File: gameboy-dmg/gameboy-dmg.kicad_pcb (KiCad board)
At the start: 2 copper layers, 82 x 63.5 mm, 27 parts, among them J1 Conn_01x02, J2 Conn_01x06, J3 Conn_01x02, SW1 SW_Push, SW2 SW_Push, SW3 SW_Push, SW4 SW_Push, SW5 SW_Push, SW6 SW_Push, SW7 SW_Push, SW8 SW_Push, U1 MCP23017_SO

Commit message: Added some graphics and stuffs
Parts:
- added G***: LOGO, pad:Tux, B.Cu at (135.7, 106.8)
- added G***: LOGO, pad:RetroPie_logo, B.Cu at (180.5, 102.5)
- C1: value C_Small -> 33nF
- C2: value C_Small -> 10uF
- R1: value R -> 270R
- R2: value R -> 150R
- moved J3 5.60 mm to (184.8, 75.4)
- renumbered SW8 to A1, SW7 to B1, SW3 to DOWN1, SW1 to LEFT1, SW4 to RIGHT1, SW5 to SELECT1, SW6 to START1, SW2 to UP1
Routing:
- net Net-(J3-Pad1): track 16.8 -> 20.9 mm
- net Net-(J3-Pad2): track 14.1 -> 17.2 mm
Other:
- board text added: "5V POWAH"
- board text added: "EXTRA BUTTONS"
- board text added: "GROUND"
- board text added: "INTERRUPT A"
- board text added: "INTERRUPT B"
- board text added: "SCK"
- board text added: "SDA"

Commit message: Added some more bits
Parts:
- added D1: LED, LED_SMD:LED_0603_1608Metric, F.Cu at (133.7, 72.2)
- added D2: LED, LED_THT:LED_D3.0mm, F.Cu at (134.9, 65.2)
- added J4: Conn_01x02, Connector_PinHeader_2.54mm:PinHeader_1x02_P2.54mm_Vertical, F.Cu at (127.3, 119.9)
- added J5: Raspberry_Pi_2_3, Connector_PinHeader_2.54mm:PinHeader_2x20_P2.54mm_Vertical, F.Cu at (185.9, 72.6)
- added J6: Conn_01x09, Connector_PinHeader_2.54mm:PinHeader_1x09_P2.54mm_Vertical, F.Cu at (147.8, 79.3)
- added JP1: SolderJumper_2_Bridged, Jumper:SolderJumper-2_P1.3mm_Bridged_RoundedPad1.0x1.5mm, F.Cu at (133.1, 78.3)
- added JP2: SolderJumper_2_Open, Jumper:SolderJumper-2_P1.3mm_Open_RoundedPad1.0x1.5mm, F.Cu at (184.8, 89.4)
- added JP3: SolderJumper_2_Open, Jumper:SolderJumper-2_P1.3mm_Open_RoundedPad1.0x1.5mm, F.Cu at (184.8, 85.3)
- added JP4: SolderJumper_2_Open, Jumper:SolderJumper-2_P1.3mm_Open_RoundedPad1.0x1.5mm, F.Cu at (179.0, 85.3)
- added JP5: SolderJumper_2_Open, Jumper:SolderJumper-2_P1.3mm_Open_RoundedPad1.0x1.5mm, F.Cu at (179.0, 89.6)
- added JP6: SolderJumper_2_Open, Jumper:SolderJumper-2_P1.3mm_Open_RoundedPad1.0x1.5mm, F.Cu at (142.3, 80.9)
- added JP7: SolderJumper_2_Bridged, Jumper:SolderJumper-2_P1.3mm_Bridged_RoundedPad1.0x1.5mm, F.Cu at (142.3, 78.4)
- added JP8: SolderJumper_2_Open, Jumper:SolderJumper-2_P1.3mm_Open_RoundedPad1.0x1.5mm, F.Cu at (129.4, 73.4)
- added R3: R_Small, Resistor_SMD:R_0603_1608Metric, F.Cu at (131.8, 72.2)
- added REF**: MountingHole_4.5mm, MountingHole:MountingHole_4.5mm, F.Cu at (127.5, 62.5)
- added REF**: MountingHole_4.5mm, MountingHole:MountingHole_4.5mm, F.Cu at (201.5, 62.5)
- added SW1: SW_DIP_x01, Connector_PinHeader_2.54mm:PinHeader_1x02_P2.54mm_Vertical, F.Cu at (125.8, 74.0)
- C2: moved to F.Cu
- J2: value Conn_01x06 -> Conn_01x02; footprint Connector_PinHeader_2.54mm:PinHeader_1x06_P2.54mm_Vertical -> Connector_PinHeader_2.54mm:PinHeader_1x02_P2.54mm_Vertical
- moved J2 60.7 mm to (142.5, 133.3), turned to 270 degrees
- moved R1 25.0 mm to (161.5, 125.5), turned to 90 degrees
- moved C2 24.5 mm to (163.2, 131.9), turned to 90 degrees
- moved C1 24.0 mm to (162.6, 122.9)
- moved R2 23.0 mm to (163.8, 125.5), turned to 90 degrees
- moved J1 18.5 mm to (168.0, 126.5), turned to 165 degrees
- moved J3 13.2 mm to (196.8, 80.8), turned to 180 degrees
- moved U1 11.0 mm to (164.4, 97.7), turned to 180 degrees
- moved G*** 6.02 mm to (176.5, 107.0)
- moved G*** 0.22 mm to (135.9, 106.7)
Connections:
- J1 pad 2: /PWM_IN -> GND
- J2 pad 1: +5V -> GND
- J2 pad 2: GND -> Net-(J2-Pad2)
- U1 pad 1: /UP -> Net-(U1-Pad1)
- U1 pad 12: Net-(J2-Pad3) -> /GPIO_SCK
- U1 pad 13: Net-(J2-Pad4) -> /GPIO_SDA
- U1 pad 19: Net-(J2-Pad5) -> /GPIO_INTB
- U1 pad 2: /LEFT -> Net-(U1-Pad2)
- U1 pad 20: Net-(J2-Pad6) -> /GPIO_INTA
- U1 pad 21: Net-(J3-Pad1) -> /UP
- U1 pad 22: Net-(J3-Pad2) -> /RIGHT
- U1 pad 23: Net-(U1-Pad23) -> /LEFT
- U1 pad 24: Net-(U1-Pad24) -> /DOWN
- U1 pad 25: Net-(U1-Pad25) -> /SELECT
- U1 pad 26: Net-(U1-Pad26) -> /START
- U1 pad 27: Net-(U1-Pad27) -> /B
- U1 pad 28: Net-(U1-Pad28) -> /A
- U1 pad 3: /DOWN -> Net-(U1-Pad3)
- U1 pad 4: /RIGHT -> Net-(U1-Pad4)
- U1 pad 5: /SELECT -> Net-(U1-Pad5)
- U1 pad 6: /START -> Net-(U1-Pad6)
- U1 pad 7: /A -> Net-(J3-Pad1)
- U1 pad 8: /B -> Net-(J3-Pad2)
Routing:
- net GND: track 0.00 -> 108.1 mm, vias 0 -> 25
- net +5V: track 16.4 -> 112.4 mm, vias 0 -> 2
- net /PWM_IN: track 3.13 -> 85.2 mm
- net Net-(J2-Pad2): track 0.00 -> 74.4 mm
- net +3V3: track 0.00 -> 37.7 mm
- net /GPIO_SDA: track 0.00 -> 24.9 mm
- net /GPIO_INTA_PI: track 0.00 -> 23.6 mm
- net /GPIO_INTA: track 0.00 -> 23.3 mm
- net /GPIO_SCK: track 0.00 -> 23.1 mm
- net /GPIO_INTB: track 0.00 -> 23.1 mm
- net Net-(J2-Pad4): track 22.2 -> 0.00 mm
- net /GPIO_SCK_PI: track 0.00 -> 21.1 mm, vias 0 -> 1
- net /TFT_MISO: track 0.00 -> 20.0 mm
- net Net-(J2-Pad3): track 19.9 -> 0.00 mm
- net /SELECT: track 31.2 -> 12.2 mm
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- added copper zone on B.Cu, net GND
- added copper zone on F.Cu, net GND
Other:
- board size 82 x 63.5 mm -> 82.5 x 77.5 mm
- net class Default: trace_width 0.25 -> 0.3
- board text added: "3.3V"
- board text added: "AUDIO GND"
- board text added: "AUDIO IN"
- board text added: "Backlight GPIO | Vcc"
- board text added: "CS"
- board text added: "DC"
- board text added: "EXT LED"
- board text added: "EXT POWER SWITCH"
- board text added: "EXTRA BUTTONZ"
- board text added: "GND"
- board text added: "GPIO Expansion Enable SDA SCK"
- board text added: "GPIO Interrupt Port B Port A"
- board text added: "ILI9341 TFT"
- board text added: "LED"
- board text added: "MISO"
- board text added: "MO SI"
- board text added: "POWAH (5V)"
- board text added: "POWER SWITCH BYPASS"
- board text added: "PWM Audio Enable"
- board text added: "RESET"
- board text added: "RPi Zero"
- board text added: "Raspberry Pi Zero Gameboy DMG Shield by Alex Hoffman"
- board text added: "Speaker"
- board text added: "TUX"
- board text removed: "5V POWAH"
- board text removed: "EXTRA BUTTONS"
- board text removed: "INTERRUPT A"
- board text removed: "INTERRUPT B"
- board text removed: "SDA"

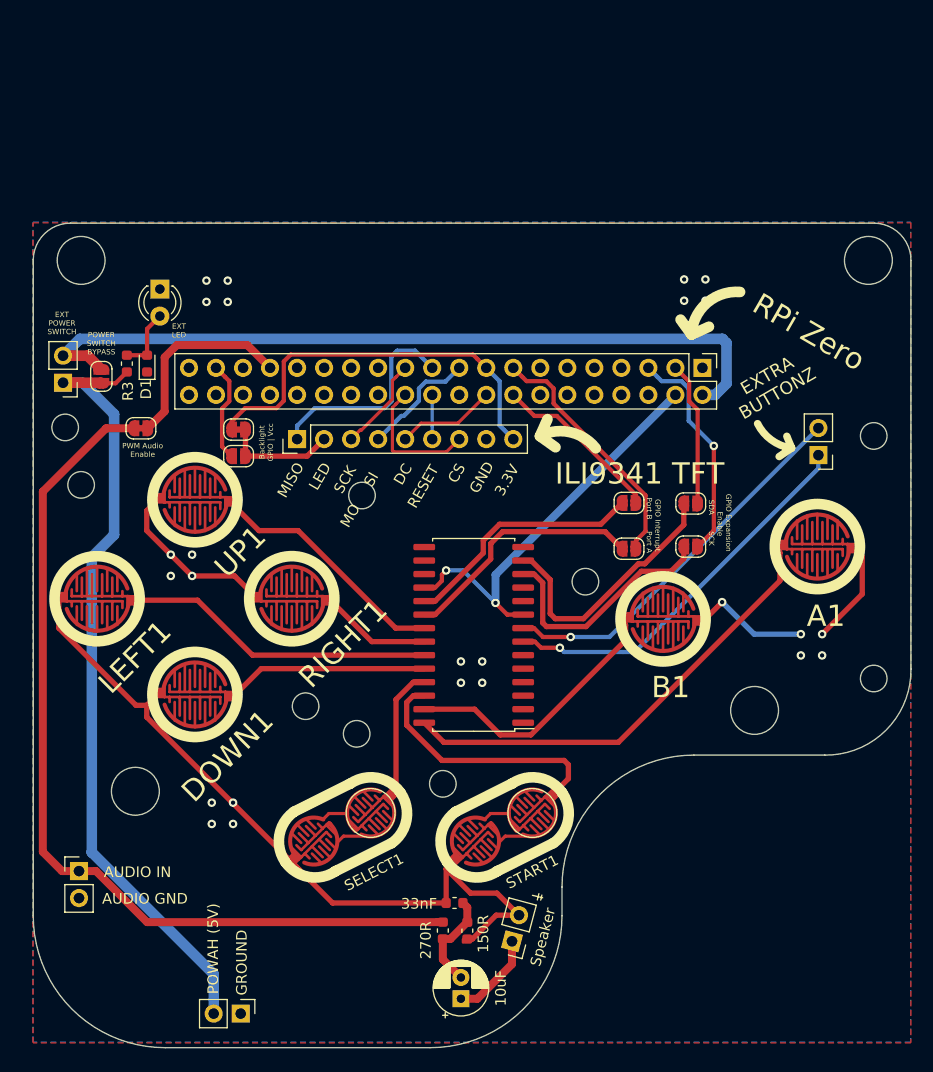
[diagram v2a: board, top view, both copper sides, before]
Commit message: Fixed some missing holes
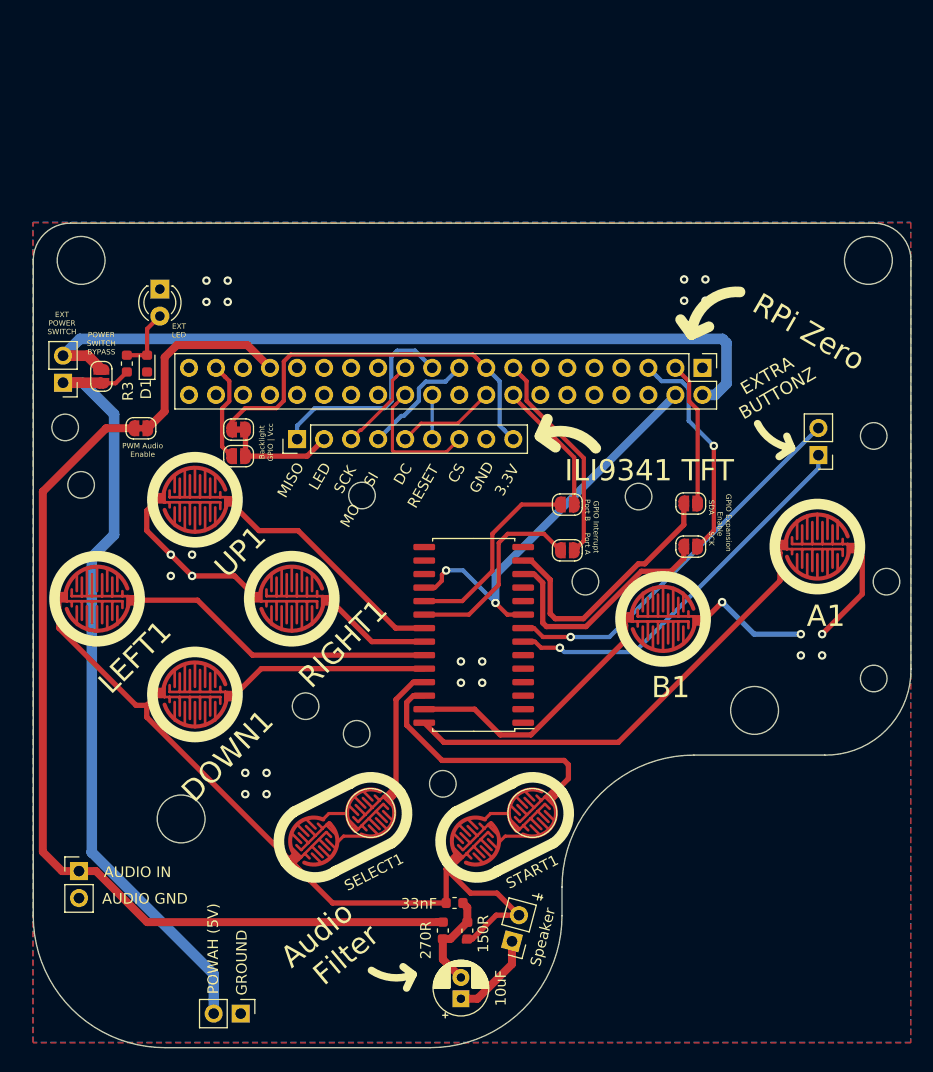
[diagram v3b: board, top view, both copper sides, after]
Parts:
- added REF**: MountingHole_2.5mm, MountingHole:MountingHole_2.5mm, F.Cu at (179.9, 84.7)
- added REF**: MountingHole_2.5mm, MountingHole:MountingHole_2.5mm, F.Cu at (203.2, 92.7)
- moved JP4 5.80 mm to (173.2, 85.5)
- moved JP5 5.80 mm to (173.2, 89.8)
- moved REF** 5.02 mm to (136.9, 115.0)
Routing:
- net /GPIO_INTB: track 23.1 -> 18.6 mm
- net /GPIO_INTA: track 23.3 -> 18.9 mm
- net /GPIO_INTB_PI: track 16.2 -> 12.7 mm
- net /GPIO_INTA_PI: track 23.6 -> 20.3 mm
- net (no net): track 0.00 -> 0.75 mm
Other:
- board text added: "Audio Filter"

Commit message: Rough lipo charger and 5v boost added
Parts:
- added C3: 0.1u, Capacitor_SMD:C_0603_1608Metric, F.Cu at (138.9, 132.2)
- added C4: 22u, Capacitor_SMD:C_1210_3225Metric, F.Cu at (125.9, 125.2)
- added C5: 10u, Capacitor_SMD:C_0603_1608Metric, F.Cu at (162.3, 128.6)
- added C6: 22u, Capacitor_SMD:C_1210_3225Metric, F.Cu at (129.3, 113.5)
- added D3: LED, LED_SMD:LED_0603_1608Metric, B.Cu at (125.5, 115.8)
- added D4: LED, LED_SMD:LED_0603_1608Metric, B.Cu at (125.5, 113.7)
- added D5: SS310, Diode_SMD:D_SMA, F.Cu at (128.2, 117.4)
- added J7: USB_B_Micro, Connector_USB:USB_Micro-B_Molex-105017-0001, F.Cu at (159.3, 132.1)
- added J8: Conn_01x02, Connector_PinHeader_2.54mm:PinHeader_1x02_P2.54mm_Vertical, F.Cu at (166.6, 132.2)
- added JP11: SolderJumper_2_Open, Jumper:SolderJumper-2_P1.3mm_Open_RoundedPad1.0x1.5mm, F.Cu at (153.1, 134.4)
- added JP9: SolderJumper_2_Open, Jumper:SolderJumper-2_P1.3mm_Open_RoundedPad1.0x1.5mm, F.Cu at (144.8, 126.5)
- added L1: 22uH, Inductor_SMD:L_7.3x7.3_H3.5, F.Cu at (137.4, 122.9)
- added R10: 1K, Resistor_SMD:R_0603_1608Metric, F.Cu at (129.6, 120.0)
- added R4: 1K, Resistor_SMD:R_0603_1608Metric, F.Cu at (151.2, 132.2)
- added R5: 1K, Resistor_SMD:R_0603_1608Metric, F.Cu at (151.2, 130.7)
- added R6: 2K, Resistor_SMD:R_0603_1608Metric, F.Cu at (138.9, 129.3)
- added R7: 100R, Resistor_SMD:R_0603_1608Metric, F.Cu at (140.4, 133.9)
- added R8: 2K, Resistor_SMD:R_0603_1608Metric, F.Cu at (130.5, 133.3)
- added R9: 7K5, Resistor_SMD:R_0603_1608Metric, F.Cu at (126.1, 120.0)
- added U2: TP4056, Package_SO:SOP-8_3.9x4.9mm_P1.27mm, F.Cu at (145.7, 130.8)
- added U3: FS312F-G, Package_TO_SOT_SMD:SOT-23-6, F.Cu at (134.3, 134.2)
- added U4: FS8205, Package_TO_SOT_SMD:SOT-23-6, F.Cu at (133.7, 130.0)
- added U5: MT3608, Package_TO_SOT_SMD:SOT-23-6, F.Cu at (129.4, 124.8)
- R3: value R_Small -> 1K
- moved J4 37.4 mm to (131.2, 82.7)
- moved J2 31.3 mm to (125.5, 107.0), turned to 0 degrees
- moved C2 15.5 mm to (149.8, 124.0), turned to 0 degrees
- moved SW1 2.95 mm to (125.7, 71.0), turned to 0 degrees
- moved JP1 2.19 mm to (135.3, 78.5)
- moved J1 1.90 mm to (169.8, 125.9), turned to 175 degrees
- moved JP8 0.75 mm to (129.3, 74.2), turned to 270 degrees
- moved G*** 0.53 mm to (135.5, 107.0)
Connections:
- J2 pad 2: Net-(J2-Pad2) -> BOOST_5V
- JP8 pad 1: Net-(J2-Pad2) -> BOOST_5V
- R3 pad 1: Net-(J2-Pad2) -> +5V
- SW1 pad 1: Net-(J2-Pad2) -> BOOST_5V
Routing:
- net Net-(J2-Pad2): track 74.4 -> 0.00 mm
- net BOOST_5V: track 0.00 -> 59.3 mm
- net /TP4056_LIPO_BOOST/BAT-: track 0.00 -> 41.9 mm, vias 0 -> 1
- net /TP4056_LIPO_BOOST/BAT+: track 0.00 -> 39.6 mm, vias 0 -> 2
- net Net-(D3-Pad2): track 0.00 -> 38.2 mm, vias 0 -> 1
- net Net-(D4-Pad1): track 0.00 -> 34.1 mm, vias 0 -> 1
- net Net-(D3-Pad1): track 0.00 -> 33.9 mm, vias 0 -> 1
- net Net-(C5-Pad1): track 0.00 -> 27.3 mm
- net /PWM_IN: track 85.2 -> 64.4 mm, vias 0 -> 1
- net Net-(C4-Pad1): track 0.00 -> 20.3 mm
- net Net-(D5-Pad2): track 0.00 -> 17.7 mm
- net /AUDIO_OUT: track 8.30 -> 22.1 mm
- net Net-(C3-Pad1): track 0.00 -> 6.43 mm
- net Net-(C1-Pad1): track 9.40 -> 15.7 mm
- net Net-(R10-Pad1): track 0.00 -> 5.69 mm
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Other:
- board text added: "+"
- board text added: "-"
- board text added: "AUDIO"
- board text added: "Battery"
- board text added: "CHARGED"
- board text added: "CHARGING"
- board text added: "Charge LEDs Enable"
- board text added: "Connect Boost"
- board text added: "EXT ON/OFF LED"
- board text added: "IN"
- board text added: "ON/OFF LED"
- board text removed: "AUDIO GND"
- board text removed: "AUDIO IN"
- board text removed: "EXT LED"

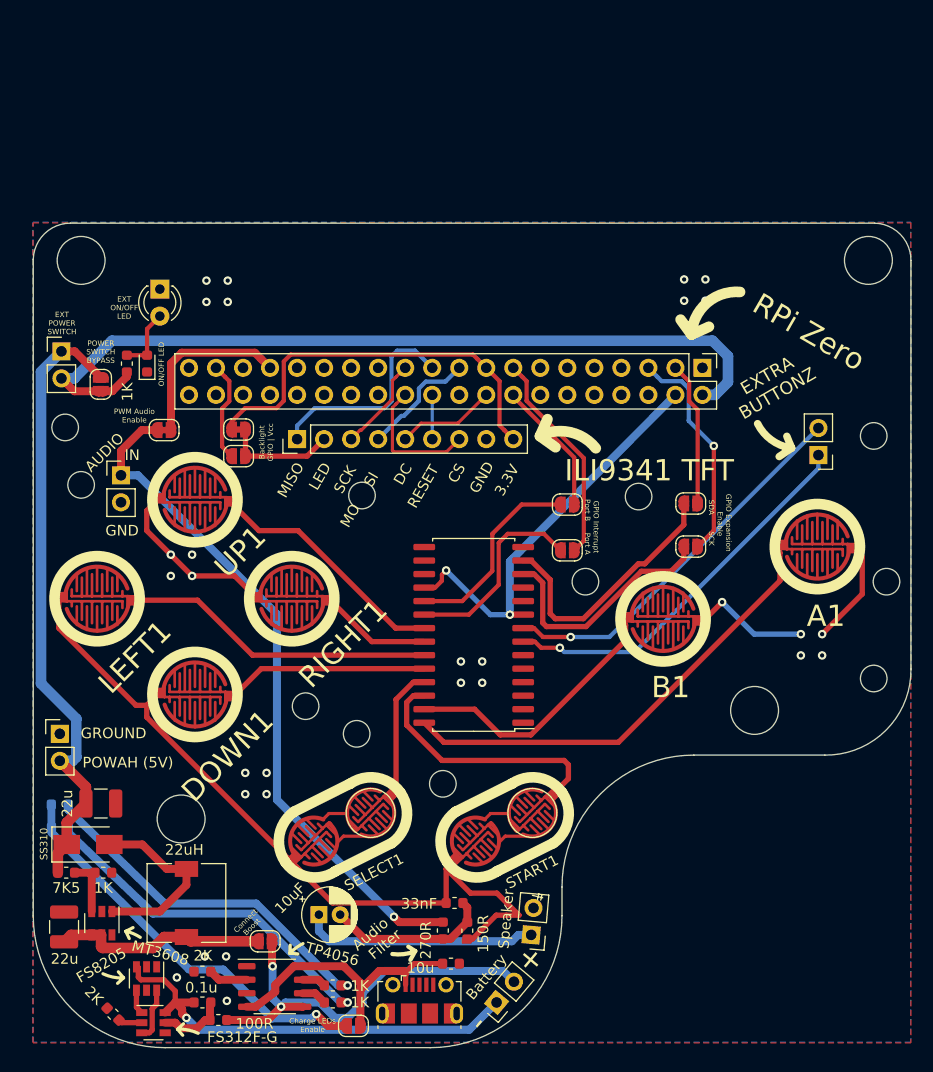
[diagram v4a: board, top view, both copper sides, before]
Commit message: Broke out all of port B to extenal pins from the MSP GPIO expander
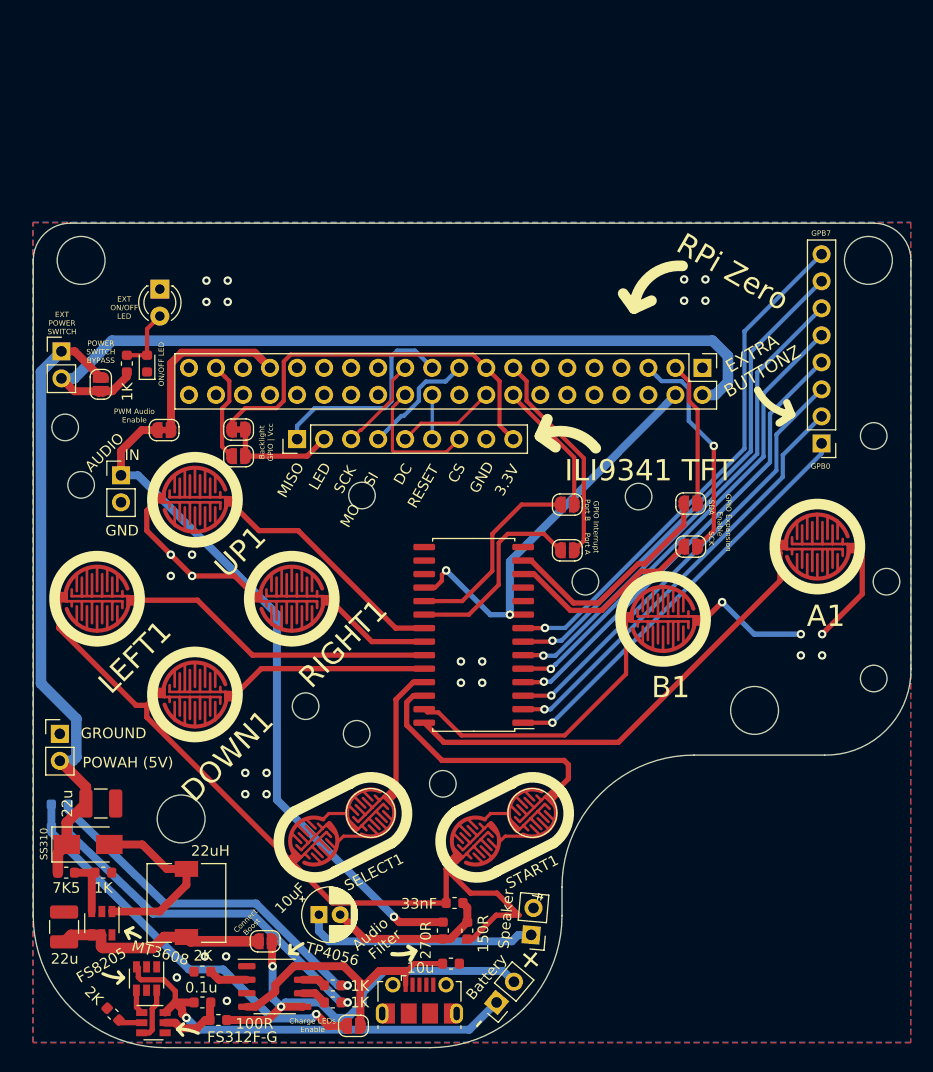
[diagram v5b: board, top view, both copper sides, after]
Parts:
- J3: value Conn_01x02 -> Conn_01x08; footprint Connector_PinHeader_2.54mm:PinHeader_1x02_P2.54mm_Vertical -> Connector_PinHeader_2.54mm:PinHeader_1x08_P2.54mm_Vertical
- moved J3 1.14 mm to (197.1, 79.7)
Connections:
- U1 pad 1: Net-(U1-Pad1) -> Net-(J3-Pad1)
- U1 pad 2: Net-(U1-Pad2) -> Net-(J3-Pad2)
- U1 pad 3: Net-(U1-Pad3) -> Net-(J3-Pad3)
- U1 pad 4: Net-(U1-Pad4) -> Net-(J3-Pad4)
- U1 pad 5: Net-(U1-Pad5) -> Net-(J3-Pad5)
- U1 pad 6: Net-(U1-Pad6) -> Net-(J3-Pad6)
- U1 pad 7: Net-(J3-Pad1) -> Net-(J3-Pad7)
- U1 pad 8: Net-(J3-Pad2) -> Net-(J3-Pad8)
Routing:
- net Net-(J3-Pad8): track 0.00 -> 49.1 mm, vias 0 -> 1
- net Net-(J3-Pad7): track 0.00 -> 47.5 mm, vias 0 -> 1
- net Net-(J3-Pad6): track 0.00 -> 46.1 mm, vias 0 -> 1
- net Net-(J3-Pad5): track 0.00 -> 44.5 mm, vias 0 -> 1
- net Net-(J3-Pad4): track 0.00 -> 43.2 mm, vias 0 -> 1
- net Net-(J3-Pad3): track 0.00 -> 42.0 mm, vias 0 -> 1
- net Net-(J3-Pad2): track 36.2 -> 40.7 mm
- net /GPIO_SCK: track 23.1 -> 19.0 mm
- net /GPIO_SDA: track 24.9 -> 21.8 mm
- net Net-(J3-Pad1): track 36.6 -> 39.5 mm
- net /B: track 25.3 -> 27.3 mm
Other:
- board text added: "GPB0"
- board text added: "GPB7"

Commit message: Cleaning up text
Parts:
- moved L1 0.71 mm to (137.5, 122.2)
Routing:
- net GND: vias 29 -> 28
